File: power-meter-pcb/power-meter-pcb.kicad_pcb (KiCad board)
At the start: 4 copper layers, 23 x 51.5 mm, 57 parts, among them J1 Crank interconnect, J2 Debug, J3 Spare GPIO pins, J4 Battery, J5 USB4120-03-C_REVA, J6 Side A, J7 Side B, Q1 AS2302, SW1 EN, SW2 BOOT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

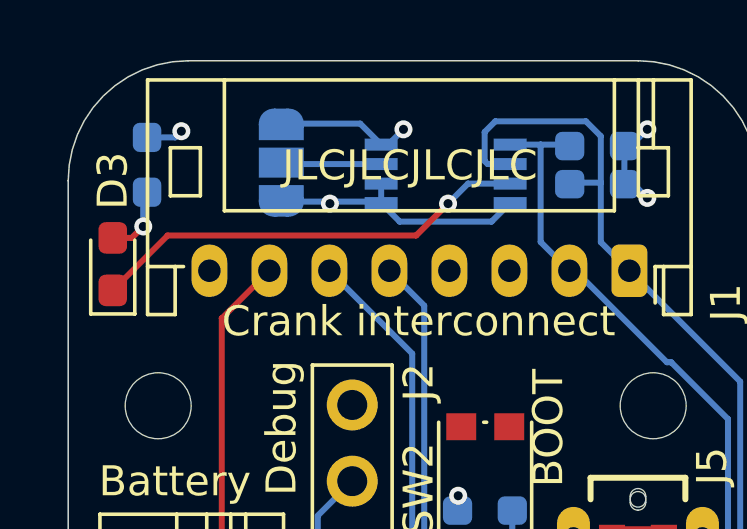
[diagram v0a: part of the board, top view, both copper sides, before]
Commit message: Fixed LED3 wiring
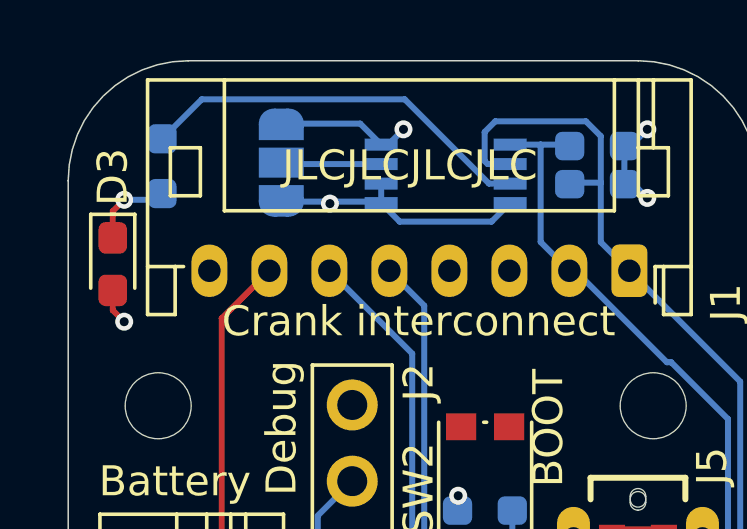
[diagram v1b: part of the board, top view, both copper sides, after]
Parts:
- moved R5 0.51 mm to (147.0, 70.6), turned to 90 degrees
- turned D3 to -90 degrees
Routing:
- net (no net): track 2.37 -> 0.00 mm
- net Net-(D3-K): track 1.23 -> 2.78 mm
- net /LED3: track 14.7 -> 13.3 mm, vias 2 -> 0
- net +3.3V: track 35.7 -> 36.9 mm, vias 9 -> 10

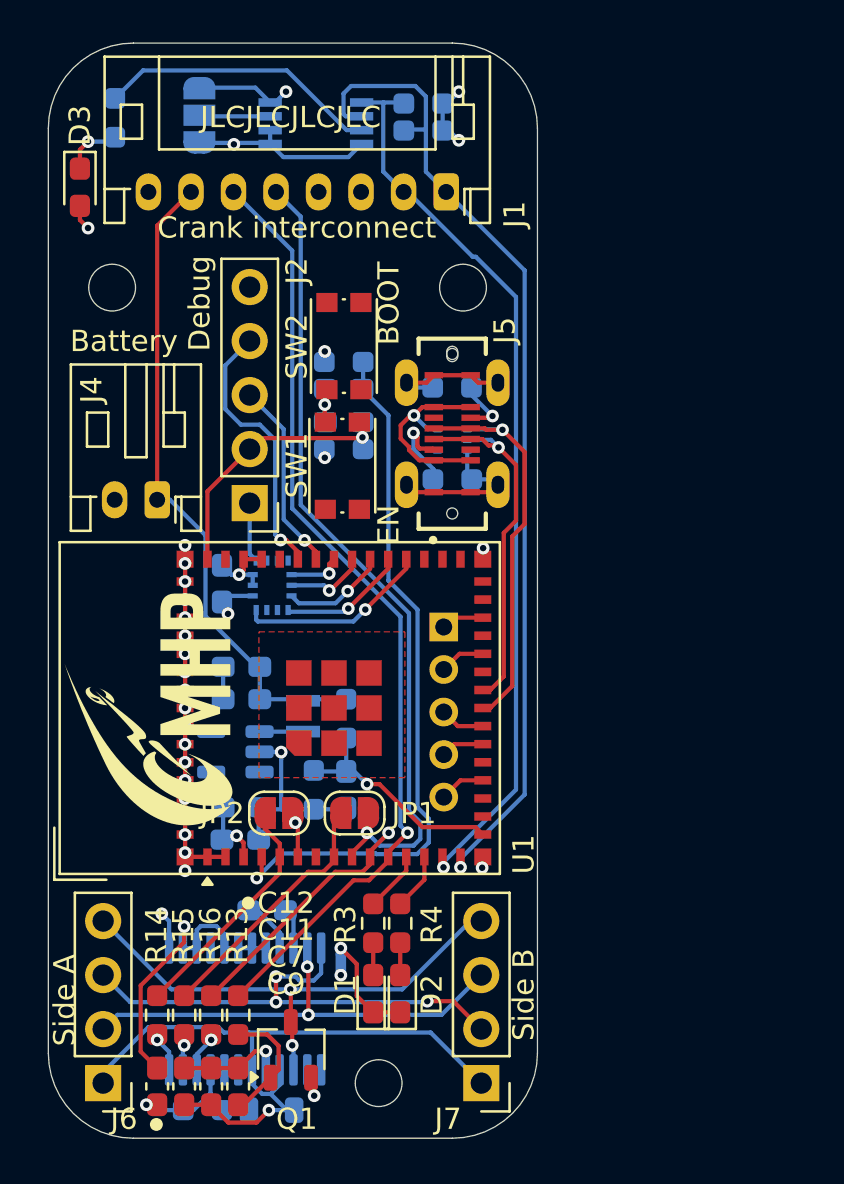
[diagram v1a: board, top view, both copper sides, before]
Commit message: Cap on ADC DC pin moved to next to pin
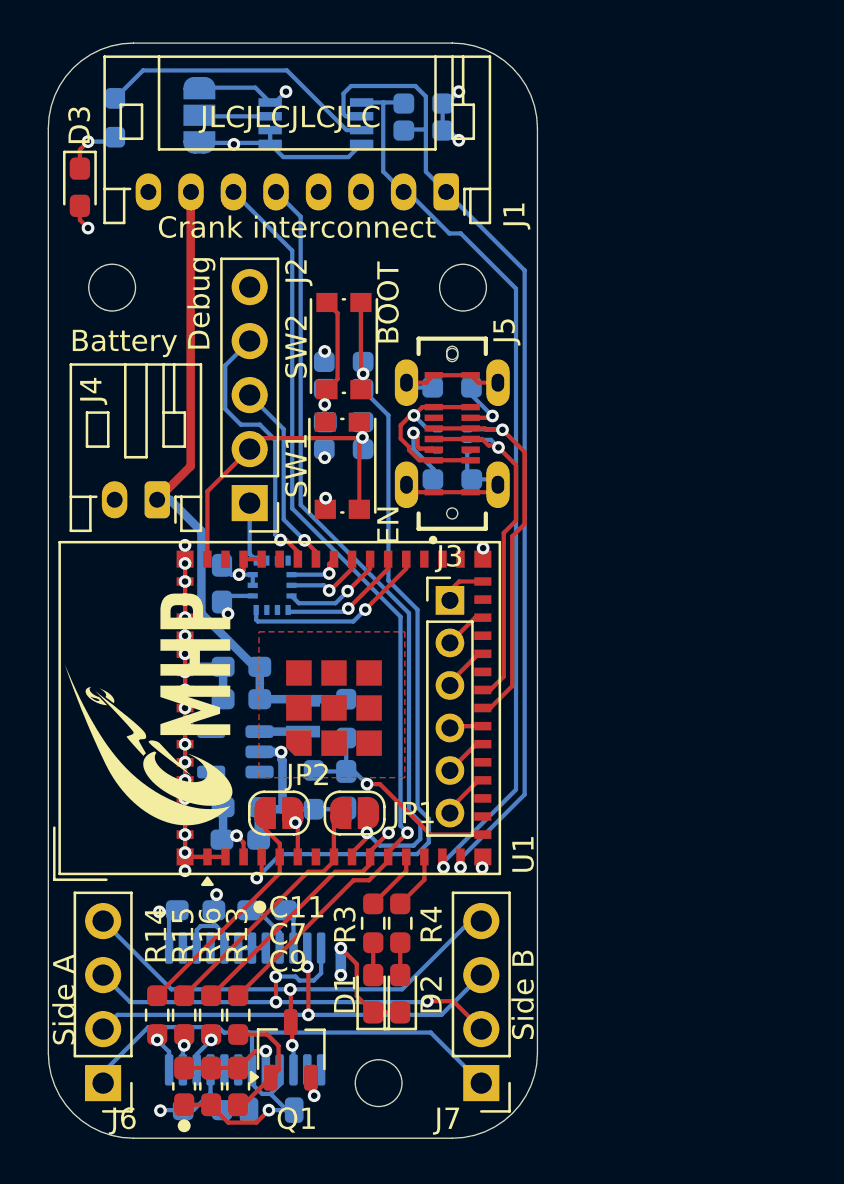
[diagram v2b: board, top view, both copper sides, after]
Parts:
- C12: moved to B.Cu
- J3: footprint Connector_PinHeader_2.00mm:PinHeader_1x05_P2.00mm_Vertical -> Connector_PinHeader_2.00mm:PinHeader_1x06_P2.00mm_Vertical; moved to F.Cu
- moved C12 8.48 mm to (150.8, 107.9), turned to 0 degrees
- moved J3 1.28 mm to (162.8, 93.3), turned to 0 degrees
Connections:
- J3 pad 1: /GPIO.33 -> /GPIO.48
- J3 pad 2: /GPIO.26 -> /GPIO.33
- J3 pad 3: /GPIO.18 -> /GPIO.26
- J3 pad 4: /GPIO.17 -> /GPIO.18
- J3 pad 5: /GPIO.15 -> /GPIO.17
- U1 pad 30: unconnected-(U1-IO48-Pad30) -> /GPIO.48
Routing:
- net /BOOT: track 33.8 -> 38.6 mm, vias 1 -> 2
- net /EN: track 12.8 -> 16.3 mm
- net /GPIO.48: track 0.00 -> 2.30 mm
- net GNDD: track 78.4 -> 76.6 mm, vias 27 -> 28
- net /GPIO.15: track 2.17 -> 2.75 mm
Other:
- board text added: "${REVISION}"
- board text added: "Power cranks"
- board text removed: "Power cranks ${REVISION}"

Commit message: Fixing I2C track labelling. V1.1.0
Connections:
- J1 pad 1: /I2C.SDA -> /I2C.SCL
- J1 pad 2: /I2C.SCL -> /I2C.SDA
- R6 pad 2: /I2C.SCL -> /I2C.SDA
- R7 pad 2: /I2C.SDA -> /I2C.SCL
- U1 pad 14: /I2C.SCL -> /I2C.SDA
- U1 pad 15: /I2C.SDA -> /I2C.SCL
- U2 pad 1: /I2C.SCL -> /I2C.SDA
- U2 pad 2: /I2C.SDA -> /I2C.SCL
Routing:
- net /I2C.SDA: track 47.0 -> 42.9 mm
- net /I2C.SCL: track 42.9 -> 47.0 mm
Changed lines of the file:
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@@
 		(title "Cycling power meter FYP")
 		(date "2024-07-15")
-		(rev "V1.0.4")
+		(rev "V1.1.0")
 		(company "Monash Human Power - Jotham Gates & Oscar Varney")
 		(comment 1 "Layer: ${LAYER}")
@@
 			(remove_unused_layers no)
 			(roundrect_rratio 0.208333)
-			(net 14 "/I2C.SDA")
+			(net 12 "/I2C.SCL")
 			(pinfunction "Pin_1")
 			(pintype "passive")
@@
 			(layers "*.Cu" "*.Mask")
 			(remove_unused_layers no)
-			(net 12 "/I2C.SCL")
+			(net 14 "/I2C.SDA")
 			(pinfunction "Pin_2")
 			(pintype "passive")
@@
 			(size 0.8 0.4)
 			(layers "F.Cu" "F.Paste" "F.Mask")
-			(net 12 "/I2C.SCL")
+			(net 14 "/I2C.SDA")
 			(pinfunction "IO10")
 			(pintype "bidirectional")
@@
 			(size 0.8 0.4)
 			(layers "F.Cu" "F.Paste" "F.Mask")
-			(net 14 "/I2C.SDA")
+			(net 12 "/I2C.SCL")
 			(pinfunction "IO11")
 			(pintype "bidirectional")
@@
 			(layers "B.Cu" "B.Paste" "B.Mask")
 			(roundrect_rratio 0.25)
-			(net 12 "/I2C.SCL")
+			(net 14 "/I2C.SDA")
 			(pintype "passive")
 		)
@@
 			(size 1.1 0.4)
 			(layers "B.Cu" "B.Paste" "B.Mask")
-			(net 12 "/I2C.SCL")
+			(net 14 "/I2C.SDA")
 			(pinfunction "SDA")
 			(pintype "bidirectional")
@@
 			(size 1.1 0.4)
 			(layers "B.Cu" "B.Paste" "B.Mask")
-			(net 14 "/I2C.SDA")
+			(net 12 "/I2C.SCL")
 			(pinfunction "SCL")
 			(pintype "input")
@@
 		)
 		(property "Value" "0.1u"
-			(at 0 -1.43 360)
+			(at 0 -1.43 0)
 			(layer "B.Fab")
 			(effects
@@
 		)
 		(fp_text user "${REFERENCE}"
-			(at 0 0 360)
+			(at 0 0 0)
 			(layer "B.Fab")
 			(effects
@@
 			(layers "B.Cu" "B.Paste" "B.Mask")
 			(roundrect_rratio 0.25)
-			(net 14 "/I2C.SDA")
+			(net 12 "/I2C.SCL")
 			(pintype "passive")
 		)
@@
 		(layer "Edge.Cuts")
 	)
-	(gr_text "SDA"
+	(gr_text "SCL"
 		(at 164.0938 74.032075 90)
 		(layer "B.SilkS")
@@
 		)
 	)
-	(gr_text "SCL"
+	(gr_text "SDA"
 		(at 160.5378 74.921075 90)
 		(layer "B.SilkS")
@@
 	)
 	(segment
-		(start 162.4328 105.833678)
-		(end 162.4328 105.393275)
-		(width 0.2)
-		(layer "F.Cu")
-		(net 12)
-	)
-	(segment
-		(start 162.482797 105.883675)
-		(end 162.4328 105.833678)
+		(start 163.2828 105.883675)
+		(end 163.2828 105.393275)
 		(width 0.2)
 		(layer "F.Cu")
@@
 	)
 	(via
-		(at 162.482797 105.883675)
+		(at 163.2828 105.883675)
 		(size 0.6)
 		(drill 0.3)
@@
 	)
 	(segment
-		(start 160.8068 74.123275)
-		(end 160.6068 74.123275)
+		(start 158.1378 69.142275)
+		(end 161.1598 69.142275)
 		(width 0.2)
 		(layer "B.Cu")
@@
 	)
 	(segment
-		(start 162.482797 105.883675)
-		(end 162.482797 105.640478)
+		(start 161.6553 73.171775)
+		(end 162.6068 74.123275)
 		(width 0.2)
 		(layer "B.Cu")
@@
 	)
 	(segment
-		(start 163.2936 76.076)
-		(end 162.759525 76.076)
+		(start 157.7828 70.467275)
+		(end 157.7828 69.497275)
 		(width 0.2)
 		(layer "B.Cu")
@@
 	)
 	(segment
-		(start 162.759525 76.076)
-		(end 160.8068 74.123275)
+		(start 166.3008 102.457475)
+		(end 166.3008 77.817275)
 		(width 0.2)
 		(layer "B.Cu")
@@
 	)
 	(segment
-		(start 162.482797 105.640478)
-		(end 165.8936 102.229675)
+		(start 157.8828 70.567275)
+		(end 157.7828 70.467275)
 		(width 0.2)
 		(layer "B.Cu")
@@
 	)
 	(segment
-		(start 159.6488 69.917275)
-		(end 159.6488 73.165275)
+		(start 161.6553 69.637775)
+		(end 161.6553 71.187275)
 		(width 0.2)
 		(layer "B.Cu")
@@
 	)
 	(segment
-		(start 159.6488 73.165275)
-		(end 160.6068 74.123275)
+		(start 163.2828 105.883675)
+		(end 163.2828 105.475475)
 		(width 0.2)
 		(layer "B.Cu")
@@
 	)
 	(segment
-		(start 159.6488 69.917275)
-		(end 160.6178 69.917275)
+		(start 161.6553 71.187275)
+		(end 160.6178 71.187275)
 		(width 0.2)
 		(layer "B.Cu")
@@
 	)
 	(segment
-		(start 158.6328 69.917275)
-		(end 159.6488 69.917275)
+		(start 157.7828 69.497275)
+		(end 158.1378 69.142275)
 		(width 0.2)
 		(layer "B.Cu")
@@
 	)
 	(segment
-		(start 165.8936 78.676)
-		(end 163.2936 76.076)
+		(start 163.2828 105.475475)
+		(end 166.3008 102.457475)
 		(width 0.2)
 		(layer "B.Cu")
@@
 	)
 	(segment
-		(start 165.8936 102.229675)
-		(end 165.8936 78.676)
+		(start 166.3008 77.817275)
+		(end 162.6068 74.123275)
+		(width 0.2)
+		(layer "B.Cu")
+		(net 12)
+	)
+	(segment
+		(start 161.1598 69.142275)
+		(end 161.6553 69.637775)
+		(width 0.2)
+		(layer "B.Cu")
+		(net 12)
+	)
+	(segment
+		(start 158.6328 70.567275)
+		(end 157.8828 70.567275)
+		(width 0.2)
+		(layer "B.Cu")
+		(net 12)
+	)
+	(segment
+		(start 161.6553 71.187275)
+		(end 161.6553 73.171775)
 		(width 0.2)
 		(layer "B.Cu")
@@
 	)
 	(segment
-		(start 163.2828 105.883675)
-		(end 163.2828 105.393275)
+		(start 162.4328 105.833678)
+		(end 162.4328 105.393275)
 		(width 0.2)
 		(layer "F.Cu")
 		(net 14)
 	)
-	(via
-		(at 163.2828 105.883675)
-		(size 0.6)
-		(drill 0.3)
-		(layers "F.Cu" "B.Cu")
-		(net 14)
-	)
 	(segment
-		(start 158.1378 69.142275)
-		(end 161.1598 69.142275)
-		(width 0.2)
-		(layer "B.Cu")
-		(net 14)
-	)
-	(segment
-		(start 161.6553 73.171775)
-		(end 162.6068 74.123275)
+		(start 162.482797 105.883675)
+		(end 162.4328 105.833678)
 		(width 0.2)
-		(layer "B.Cu")
+		(layer "F.Cu")
 		(net 14)
 	)
-	(segment
-		(start 157.7828 70.467275)
-		(end 157.7828 69.497275)
-		(width 0.2)
-		(layer "B.Cu")
+	(via
+		(at 162.482797 105.883675)
+		(size 0.6)
+		(drill 0.3)
+		(layers "F.Cu" "B.Cu")
 		(net 14)
 	)
 	(segment
-		(start 166.3008 102.457475)
-		(end 166.3008 77.817275)
+		(start 160.8068 74.123275)
+		(end 160.6068 74.123275)
 		(width 0.2)
 		(layer "B.Cu")
@@
 	)
 	(segment
-		(start 157.8828 70.567275)
-		(end 157.7828 70.467275)
+		(start 162.482797 105.883675)
+		(end 162.482797 105.640478)
 		(width 0.2)
 		(layer "B.Cu")
@@
 	)
 	(segment
-		(start 161.6553 69.637775)
-		(end 161.6553 71.187275)
+		(start 163.2936 76.076)
+		(end 162.759525 76.076)
 		(width 0.2)
 		(layer "B.Cu")
@@
 	)
 	(segment
-		(start 163.2828 105.883675)
-		(end 163.2828 105.475475)
+		(start 162.759525 76.076)
+		(end 160.8068 74.123275)
 		(width 0.2)
 		(layer "B.Cu")
@@
 	)
 	(segment
-		(start 161.6553 71.187275)
-		(end 160.6178 71.187275)
+		(start 162.482797 105.640478)
+		(end 165.8936 102.229675)
 		(width 0.2)
 		(layer "B.Cu")
@@
 	)
 	(segment
-		(start 157.7828 69.497275)
-		(end 158.1378 69.142275)
+		(start 159.6488 69.917275)
+		(end 159.6488 73.165275)
 		(width 0.2)
 		(layer "B.Cu")
@@
 	)
 	(segment
-		(start 163.2828 105.475475)
-		(end 166.3008 102.457475)
+		(start 159.6488 73.165275)
+		(end 160.6068 74.123275)
 		(width 0.2)
 		(layer "B.Cu")
@@
 	)
 	(segment
-		(start 166.3008 77.817275)
-		(end 162.6068 74.123275)
+		(start 159.6488 69.917275)
+		(end 160.6178 69.917275)
 		(width 0.2)
 		(layer "B.Cu")
@@
 	)
 	(segment
-		(start 161.1598 69.142275)
-		(end 161.6553 69.637775)
+		(start 158.6328 69.917275)
+		(end 159.6488 69.917275)
 		(width 0.2)
 		(layer "B.Cu")
@@
 	)
 	(segment
-		(start 158.6328 70.567275)
-		(end 157.8828 70.567275)
+		(start 165.8936 78.676)
+		(end 163.2936 76.076)
 		(width 0.2)
 		(layer "B.Cu")
@@
 	)
 	(segment
-		(start 161.6553 71.187275)
-		(end 161.6553 73.171775)
+		(start 165.8936 102.229675)
+		(end 165.8936 78.676)
 		(width 0.2)
 		(layer "B.Cu")

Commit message: Fixed SPI pin labels
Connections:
- MT1 pad 1: /Accelerometer/SPI.SDO -> /Accelerometer/SPI.SDI
- MT1 pad 14: /Accelerometer/SPI.SDI -> /Accelerometer/SPI.SDO
- U1 pad 35: /Accelerometer/SPI.SDO -> /Accelerometer/SPI.SDI
- U1 pad 36: /Accelerometer/SPI.SDI -> /Accelerometer/SPI.SDO
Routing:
- net /Accelerometer/SPI.SDO: track 6.03 -> 4.96 mm
- net /Accelerometer/SPI.SDI: track 4.96 -> 6.03 mm
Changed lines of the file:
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@@
 			(size 0.8 0.4)
 			(layers "F.Cu" "F.Paste" "F.Mask")
-			(net 31 "/Accelerometer/SPI.SDO")
+			(net 29 "/Accelerometer/SPI.SDI")
 			(pinfunction "IO39")
 			(pintype "bidirectional")
@@
 			(size 0.8 0.4)
 			(layers "F.Cu" "F.Paste" "F.Mask")
-			(net 29 "/Accelerometer/SPI.SDI")
+			(net 31 "/Accelerometer/SPI.SDO")
 			(pinfunction "IO40")
 			(pintype "bidirectional")
@@
 			(size 0.475 0.25)
 			(layers "B.Cu")
-			(net 31 "/Accelerometer/SPI.SDO")
+			(net 29 "/Accelerometer/SPI.SDI")
 			(pinfunction "AP_SDO/AP_AD0")
 			(pintype "bidirectional")
@@
 			(size 0.25 0.475)
 			(layers "B.Cu")
-			(net 29 "/Accelerometer/SPI.SDI")
+			(net 31 "/Accelerometer/SPI.SDO")
 			(pinfunction "AP_SDA/AP_SDIO/AP_SDI")
 			(pintype "bidirectional")
@@
 	)
 	(segment
-		(start 157.976757 92.895177)
-		(end 159.0328 91.839134)
+		(start 159.8828 91.837663)
+		(end 159.8828 91.393275)
 		(width 0.2)
 		(layer "F.Cu")
@@
 	)
 	(segment
-		(start 159.0328 91.839134)
-		(end 159.0328 91.393275)
+		(start 158.005922 93.714541)
+		(end 159.8828 91.837663)
 		(width 0.2)
 		(layer "F.Cu")
@@
 	)
 	(via
-		(at 157.976757 92.895177)
+		(at 158.005922 93.714541)
 		(size 0.6)
 		(drill 0.3)
@@
 	)
 	(segment
-		(start 157.405856 93.466078)
-		(end 155.682478 93.466078)
+		(start 155.17505 93.78365)
+		(end 155.257478 93.866078)
 		(width 0.2)
 		(layer "B.Cu")
@@
 	)
 	(segment
-		(start 155.682478 93.466078)
-		(end 155.33755 93.12115)
+		(start 157.854385 93.866078)
+		(end 158.005922 93.714541)
 		(width 0.2)
 		(layer "B.Cu")
@@
 	)
 	(segment
-		(start 157.976757 92.895177)
-		(end 157.405856 93.466078)
+		(start 155.257478 93.866078)
+		(end 157.854385 93.866078)
 		(width 0.2)
 		(layer "B.Cu")
@@
 	)
 	(segment
-		(start 159.8828 91.837663)
-		(end 159.8828 91.393275)
+		(start 157.976757 92.895177)
+		(end 159.0328 91.839134)
 		(width 0.2)
 		(layer "F.Cu")
@@
 	)
 	(segment
-		(start 158.005922 93.714541)
-		(end 159.8828 91.837663)
+		(start 159.0328 91.839134)
+		(end 159.0328 91.393275)
 		(width 0.2)
 		(layer "F.Cu")
@@
 	)
 	(via
-		(at 158.005922 93.714541)
+		(at 157.976757 92.895177)
 		(size 0.6)
 		(drill 0.3)
@@
 	)
 	(segment
-		(start 155.17505 93.78365)
-		(end 155.257478 93.866078)
+		(start 157.405856 93.466078)
+		(end 155.682478 93.466078)
 		(width 0.2)
 		(layer "B.Cu")
@@
 	)
 	(segment
-		(start 157.854385 93.866078)
-		(end 158.005922 93.714541)
+		(start 155.682478 93.466078)
+		(end 155.33755 93.12115)
 		(width 0.2)
 		(layer "B.Cu")
@@
 	)
 	(segment
-		(start 155.257478 93.866078)
-		(end 157.854385 93.866078)
+		(start 157.976757 92.895177)
+		(end 157.405856 93.466078)
 		(width 0.2)
 		(layer "B.Cu")

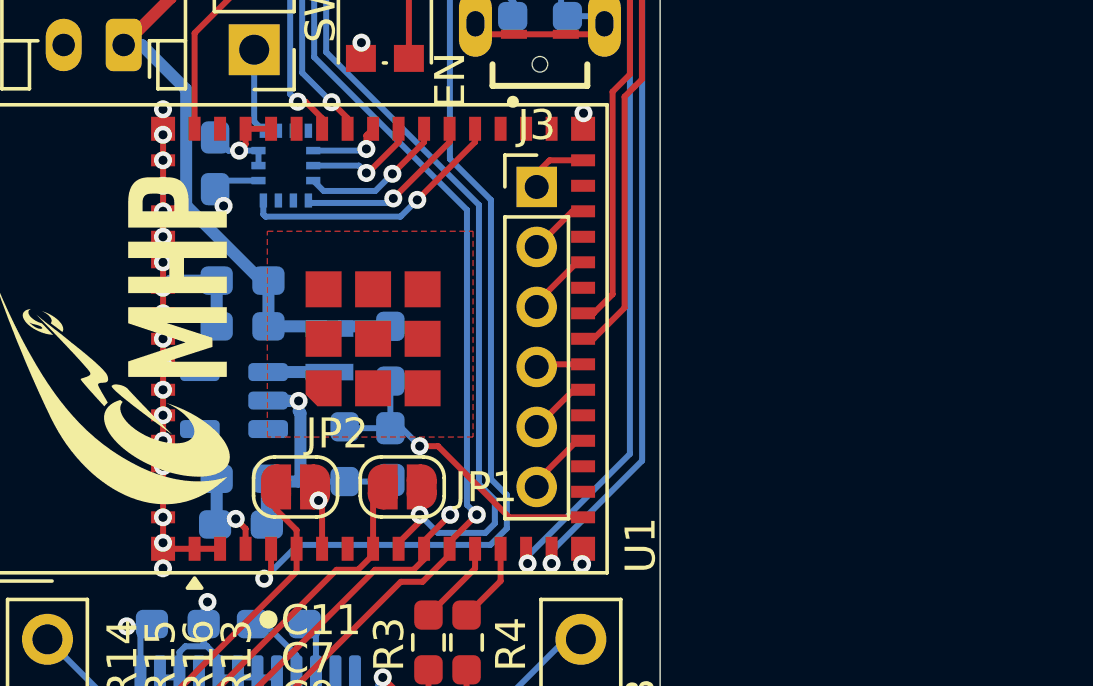
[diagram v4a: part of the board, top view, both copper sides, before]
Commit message: Uses a TPS61022 Voltage regulator - will change for easier soldering
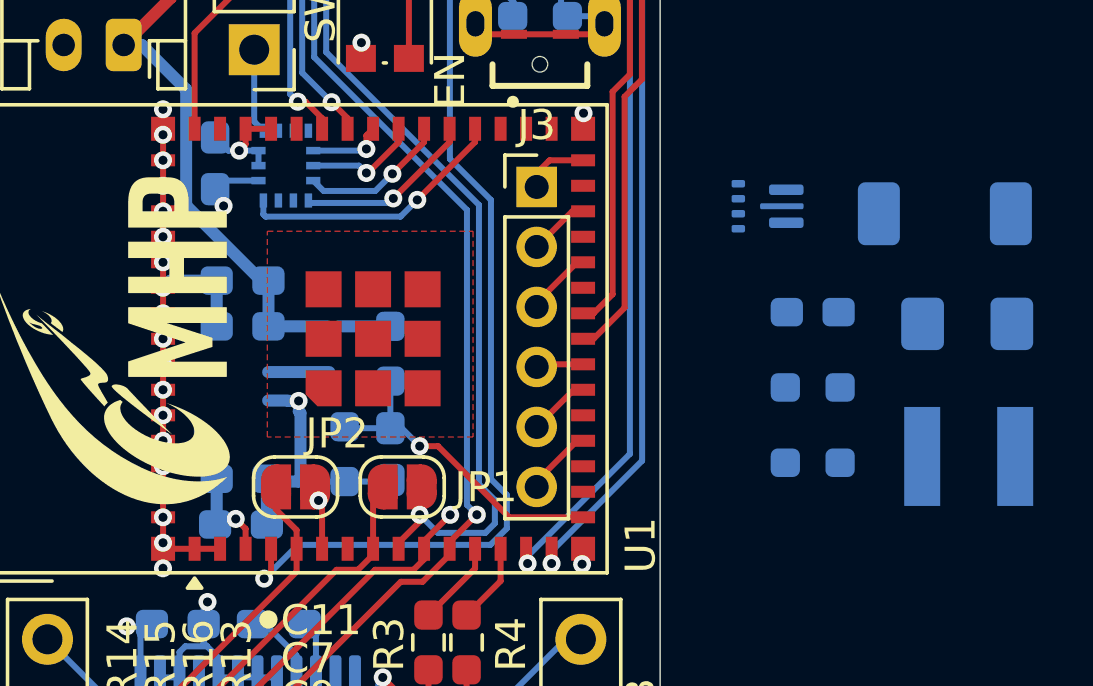
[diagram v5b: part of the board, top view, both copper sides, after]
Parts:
- added C14: 22u, Capacitor_SMD:C_0603_1608Metric_Pad1.08x0.95mm_HandSolder, B.Cu at (172.0, 97.5)
- added D4: PMEG6030ELPX, Diode_SMD:D_SOD-128, B.Cu at (176.4, 94.2)
- added F1: SMD1206B200TF, Fuse:Fuse_1206_3216Metric_Pad1.42x1.75mm_HandSolder, B.Cu at (177.1, 97.9)
- added R17: 453k, Resistor_SMD:R_0603_1608Metric_Pad0.98x0.95mm_HandSolder, B.Cu at (172.0, 100.0)
- added R18: 100k, Resistor_SMD:R_0603_1608Metric_Pad0.98x0.95mm_HandSolder, B.Cu at (172.0, 102.5)
- C3, C5, C6: value 10u -> 22u
- C4: value 0.1u -> 22u
- L1: value 4.7uH -> 1u; footprint Inductor_SMD:L_Murata_DFE201610P -> Inductor_SMD_Wurth:L_Wurth_WE-LQSH-4020
- U3: value TPS613221ADBV -> TPS61022; footprint Package_TO_SOT_SMD:SOT-23-5 -> Package_DFN_QFN:Texas_RWU0007A_VQFN-7_2x2mm_P0.5mm
- moved L1 21.6 mm to (177.2, 102.3), turned to 180 degrees
- moved U3 18.9 mm to (170.5, 94.0)
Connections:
- J4 pad 1: +BATT -> Net-(J4-+)
- U3 pad 1: Net-(U3-SW) -> GNDD
- U3 pad 2: GNDD -> Net-(U3-SW)
- U3 pad 3: unconnected-(U3-NC-Pad3) -> +3.3V
- U3 pad 4: +3.3V -> Net-(U3-FB)
- U3 pad 5: unconnected-(U3-NC-Pad5) -> +BATT
